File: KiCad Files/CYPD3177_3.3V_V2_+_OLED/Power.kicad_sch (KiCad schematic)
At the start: 37 parts, among them J1 USB_C_Receptacle_USB2.0_14P, J2 Conn_01x02_Pin, J3 Conn_02x05_Odd_Even, J4 Conn_02x05_Odd_Even, U3 XC6220B331PR-G, U4 TPS62933DRLR, U5 AON7534, U6 AP33772S, U7 AON7534

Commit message: changes
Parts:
- renumbered C8 to C17
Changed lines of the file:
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@@
 		(on_board yes)
 		(dnp no)
-		(property "Reference" "C8"
+		(property "Reference" "C17"
 			(at 76.2 161.29 0)
 			(effects
@@
 			(project "CYPD3177_3.3V_V2_+_OLED"
 				(path "/a370047b-ebc6-4236-825e-9462ba7e4392/f9278a29-edee-4e3c-b24d-7a370e39fb32"
-					(reference "C8")
+					(reference "C17")
 					(unit 1)
 				)

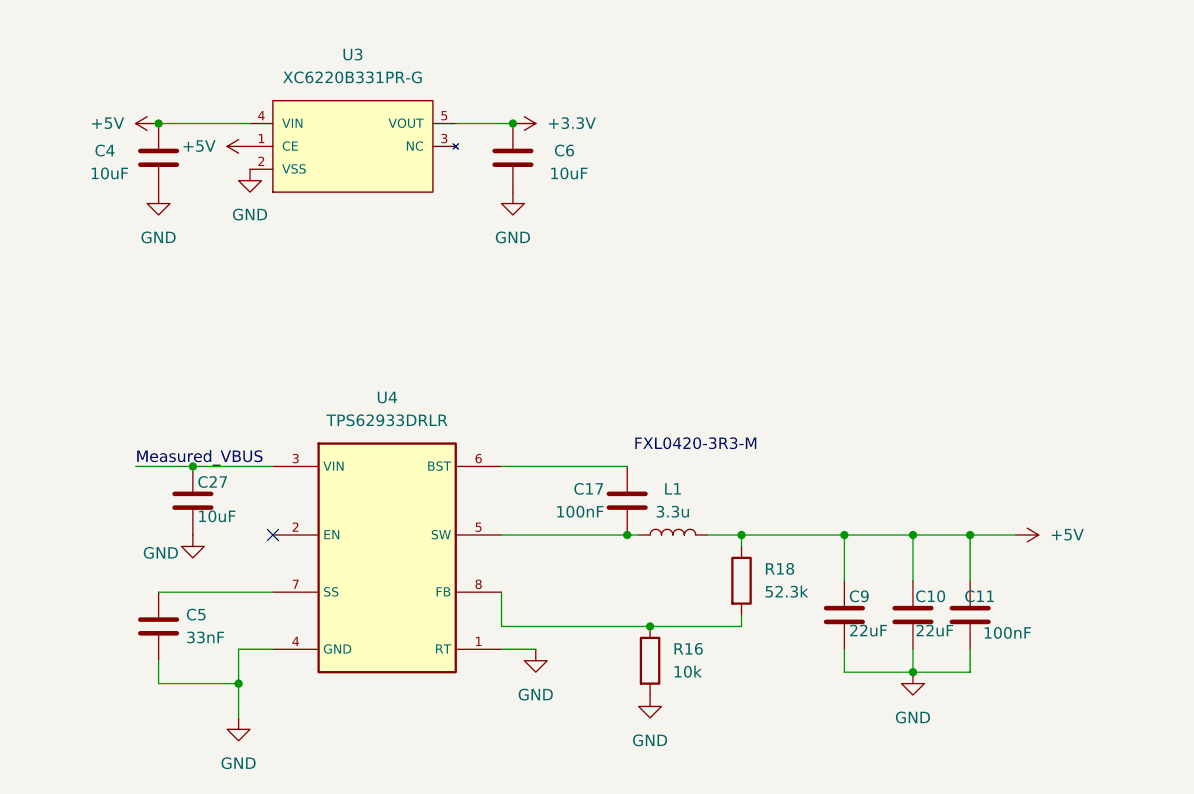
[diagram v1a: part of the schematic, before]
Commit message: finshed pcb, assigning part numbers
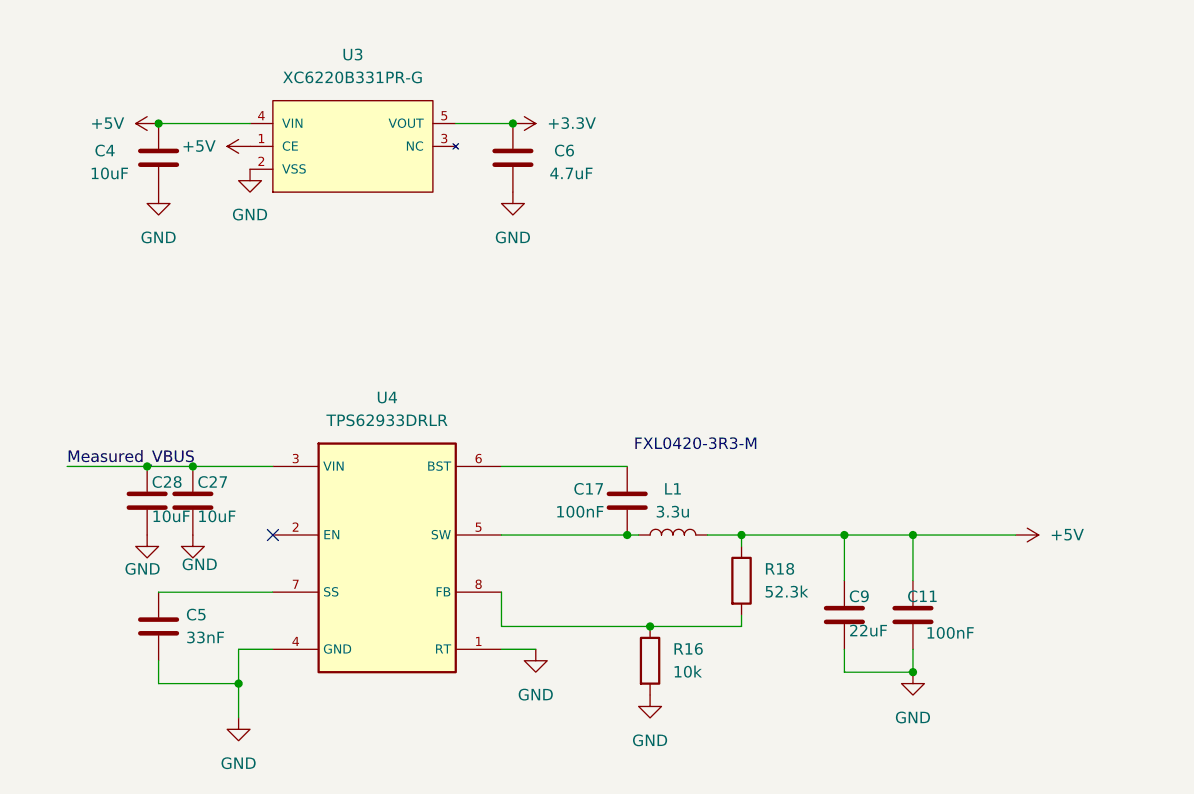
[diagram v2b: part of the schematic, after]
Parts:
- removed C10: 22uF, Capacitor_SMD:C_1206_3216Metric, symbol Device:C
- added C28: 10uF, Capacitor_SMD:C_1206_3216Metric, symbol Device:C
- C4: footprint Capacitor_SMD:C_0402_1005Metric -> Capacitor_SMD:C_0603_1608Metric; LCSC C513774 -> (none)
- C6: value 10uF -> 4.7uF
- C7: footprint Capacitor_SMD:C_0805_2012Metric_Pad1.18x1.45mm_HandSolder -> Capacitor_SMD:C_1206_3216Metric
- R17: footprint Inductor_SMD:L_1206_3216Metric_Pad1.42x1.75mm_HandSolder -> Resistor_SMD:R_1206_3216Metric
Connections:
- net GND: now also C28.2
- net Measured_VBUS: now also C28.1
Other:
- moved on the sheet: C11

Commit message: changes
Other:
- title: (none) -> USB PD PPS for breadboards
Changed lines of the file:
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@@
 	(generator_version "9.0")
 	(paper "A4")
+	(title_block
+		(title "USB PD PPS for breadboards")
+		(date "2025-05-01")
+		(rev "V1")
+		(comment 1 "Licensed under CC BY-NC-SA 4.0 (c) 2025 Shinui")
+	)
 	(text "FXL0420-3R3-M "
 		(exclude_from_sim no)

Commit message: almost finished
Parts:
- added D7: PMEG6020ER, Diode_SMD:D_SOD-123F, symbol Diode:PMEG6020ER
- D4: value RED or BLUE -> White Status LED
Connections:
- net +5V: now also D7.2 (A)
- net Measured_VBUS: now also D7.1 (K)
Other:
- note added: "Buck Converter for VBUS -> 5V"
- note added: "ESD protection"
- note added: "FXL0420-3R3-M (power inductor)"
- note added: "Pin headers to plug into breaboard"
- note added: "Screw terminal"
- note removed: "C5349543"
- note removed: "FXL0420-3R3-M"
- moved on the sheet: D3, J4

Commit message: now final version, changed routing completly and should be better board
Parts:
- renumbered C9 to C10
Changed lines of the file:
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@@
 		(on_board yes)
 		(dnp no)
-		(property "Reference" "C9"
+		(property "Reference" "C10"
 			(at 103.378 173.228 0)
 			(effects
@@
 			(project "CYPD3177_3.3V_V2_+_OLED"
 				(path "/a370047b-ebc6-4236-825e-9462ba7e4392/f9278a29-edee-4e3c-b24d-7a370e39fb32"
-					(reference "C9")
+					(reference "C10")
 					(unit 1)
 				)

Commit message: changes
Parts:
- added U10: TPS62933P, Package_TO_SOT_SMD:SOT-583-8, symbol Regulator_Switching:TPS62933P
- renumbered C5 to C/R5
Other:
- note added: "This component(C/R5) can either be 33nF cap for ..62933DR or a 10k Resistor for ..33PDR."
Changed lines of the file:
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@@
 		)
 	)
+	(text "This component(C/R5) can either be 33nF cap for ..62933DR \nor a 10k Resistor for ..33PDR."
+		(exclude_from_sim no)
+		(at -6.604 177.8 0)
+		(effects
+			(font
+				(size 1.27 1.27)
+			)
+		)
+	)
 	(text "Buck Converter for VBUS -> 5V"
 		(exclude_from_sim no)
@@
 	)
 	(symbol
+		(lib_id "Regulator_Switching:TPS62933P")
+		(at 52.07 194.31 0)
+		(unit 1)
+		(exclude_from_sim no)
+		(in_bom yes)
+		(on_board yes)
+		(dnp no)
+		(fields_autoplaced yes)
+		(property "Reference" "U10"
+			(at 52.07 179.07 0)
+			(effects
+				(font
+					(size 1.27 1.27)
+				)
+			)
+		)
+		(property "Value" "TPS62933P"
+			(at 52.07 181.61 0)
+			(effects
+				(font
+					(size 1.27 1.27)
+				)
+			)
+		)
+		(property "Footprint" "Package_TO_SOT_SMD:SOT-583-8"
+			(at 52.07 219.71 0)
+			(effects
+				(font
+					(size 1.27 1.27)
+				)
+				(hide yes)
+			)
+		)
+		(property "Datasheet" "https://www.ti.com/lit/ds/symlink/tps62933.pdf"
+			(at 52.07 217.17 0)
+			(effects
+				(font
+					(size 1.27 1.27)
+				)
+				(hide yes)
+			)
+		)
+		(property "Description" "3.8-30V, 3A Synchronous Buck Converters with pulse frequency modulation (PFM) and power good, SOT583-8"
+			(at 52.07 194.31 0)
+			(effects
+				(font
+					(size 1.27 1.27)
+				)
+				(hide yes)
+			)
+		)
+		(pin "5"
+		)
+		(pin "8"
+		)
+		(pin "3"
+		)
+		(pin "6"
+		)
+		(pin "7"
+		)
+		(pin "4"
+		)
+		(pin "2"
+		)
+		(pin "1"
+		)
+		(instances
+			(project ""
+				(path "/a370047b-ebc6-4236-825e-9462ba7e4392/f9278a29-edee-4e3c-b24d-7a370e39fb32"
+					(reference "U10")
+					(unit 1)
+				)
+			)
+		)
+	)
+	(symbol
 		(lib_id "power:GND")
 		(at 222.25 140.97 0)
@@
 		(on_board yes)
 		(dnp no)
-		(property "Reference" "C5"
+		(property "Reference" "C/R5"
 			(at 29.718 175.26 0)
 			(effects
@@
 			(project "CYPD3177_3.3V_V2_+_OLED"
 				(path "/a370047b-ebc6-4236-825e-9462ba7e4392/f9278a29-edee-4e3c-b24d-7a370e39fb32"
-					(reference "C5")
+					(reference "C/R5")
 					(unit 1)
 				)

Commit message: ff
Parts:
- removed U10: TPS62933P, Package_TO_SOT_SMD:SOT-583-8, symbol Regulator_Switching:TPS62933P
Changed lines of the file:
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@@
-	)
-	(symbol
-		(lib_id "Regulator_Switching:TPS62933P")
-		(at 52.07 194.31 0)
-		(unit 1)
-		(exclude_from_sim no)
-		(in_bom yes)
-		(on_board yes)
-		(dnp no)
-		(fields_autoplaced yes)
-		(property "Reference" "U10"
-			(at 52.07 179.07 0)
-			(effects
-				(font
-					(size 1.27 1.27)
-				)
-			)
-		)
-		(property "Value" "TPS62933P"
-			(at 52.07 181.61 0)
-			(effects
-				(font
-					(size 1.27 1.27)
-				)
-			)
-		)
-		(property "Footprint" "Package_TO_SOT_SMD:SOT-583-8"
-			(at 52.07 219.71 0)
-			(effects
-				(font
-					(size 1.27 1.27)
-				)
-				(hide yes)
-			)
-		)
-		(property "Datasheet" "https://www.ti.com/lit/ds/symlink/tps62933.pdf"
-			(at 52.07 217.17 0)
-			(effects
-				(font
-					(size 1.27 1.27)
-				)
-				(hide yes)
-			)
-		)
-		(property "Description" "3.8-30V, 3A Synchronous Buck Converters with pulse frequency modulation (PFM) and power good, SOT583-8"
-			(at 52.07 194.31 0)
-			(effects
-				(font
-					(size 1.27 1.27)
-				)
-				(hide yes)
-			)
-		)
-		(pin "5"
-		)
-		(pin "8"
-		)
-		(pin "3"
-		)
-		(pin "6"
-		)
-		(pin "7"
-		)
-		(pin "4"
-		)
-		(pin "2"
-		)
-		(pin "1"
-		)
-		(instances
-			(project ""
-				(path "/a370047b-ebc6-4236-825e-9462ba7e4392/f9278a29-edee-4e3c-b24d-7a370e39fb32"
-					(reference "U10")
-					(unit 1)
-				)
-			)
-		)
 	)
 	(symbol
